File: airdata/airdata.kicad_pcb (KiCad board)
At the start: 2 copper layers, 3 parts, among them U1 SDP32, U3 SDP32, U6 SDP32

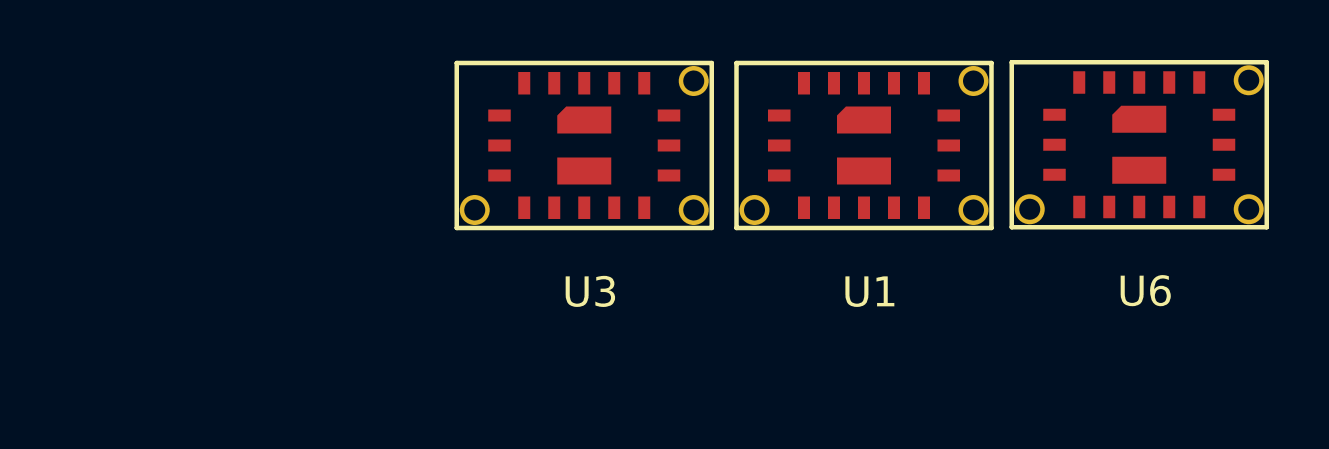
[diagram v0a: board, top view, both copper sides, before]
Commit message: airdata footprints & 3d models
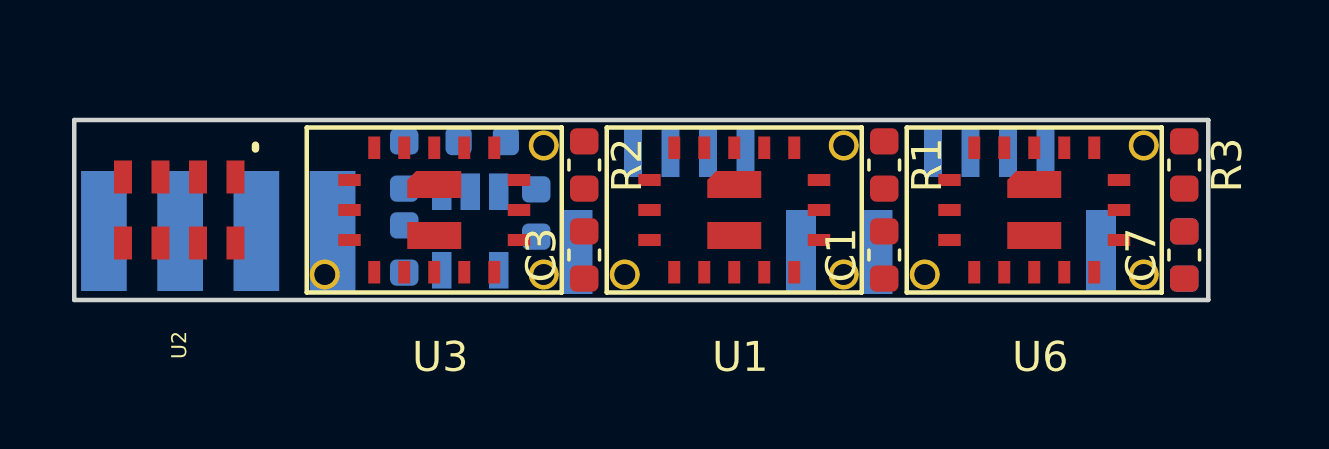
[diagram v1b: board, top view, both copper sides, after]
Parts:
- added C1: 100nF, Capacitor_SMD:C_0603_1608Metric, F.Cu at (55.0, 34.0)
- added C2: 100nF, Capacitor_SMD:C_0603_1608Metric, B.Cu at (65.0, 34.0)
- added C3: 100nF, Capacitor_SMD:C_0603_1608Metric, F.Cu at (45.0, 34.0)
- added C4: 1uF, Capacitor_SMD:C_0603_1608Metric, B.Cu at (41.6, 30.2)
- added C5: 100nF, Capacitor_SMD:C_0603_1608Metric, B.Cu at (39.0, 31.0)
- added C6: 0.01uF, Capacitor_SMD:C_0603_1608Metric, B.Cu at (43.4, 32.6)
- added C7: 100nF, Capacitor_SMD:C_0603_1608Metric, F.Cu at (65.0, 34.0)
- added C8: 10uF, Capacitor_SMD:C_0603_1608Metric, B.Cu at (39.0, 33.8)
- added J1: I2C, Connector_JST:JST_GH_BM04B-GHS-TBT_1x04-1MP_P1.25mm_Vertical, B.Cu at (58.5, 32.5)
- added J2: I2C, Connector_JST:JST_GH_BM04B-GHS-TBT_1x04-1MP_P1.25mm_Vertical, B.Cu at (48.5, 32.5)
- added R1: 0, Resistor_SMD:R_0603_1608Metric, F.Cu at (55.0, 31.0)
- added R2: 1.2k, Resistor_SMD:R_0603_1608Metric, F.Cu at (45.0, 31.0)
- added R3: 2.7k, Resistor_SMD:R_0603_1608Metric, F.Cu at (65.0, 31.0)
- added U2: MS5611-01BA03, footprints:MS5611-01BA, F.Cu at (31.5, 32.5)
- added U4: LT1761-3.3, Package_TO_SOT_SMD:TSOT-23-5, B.Cu at (41.2, 33.2)
- added U5: HSCMRRN001PD2A3, footprints:HSCMRRN001PD2A3-side-mount, B.Cu at (32.8, 33.2)
- moved U3 5.44 mm to (40.0, 32.5)
- moved U1 4.83 mm to (50.0, 32.5)
- moved U6 4.12 mm to (60.0, 32.5)
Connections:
- U1 pad 12: Net-(U1-Pad12) -> (no net)
- U1 pad 13: Net-(U1-Pad13) -> (no net)
- U1 pad 14: Net-(U1-Pad14) -> (no net)
- U1 pad 15: Net-(U1-Pad15) -> (no net)
- U1 pad 16: Net-(U1-Pad16) -> (no net)
- U1 pad 4: Net-(U1-Pad4) -> (no net)
- U3 pad 12: Net-(U3-Pad12) -> (no net)
- U3 pad 13: Net-(U3-Pad13) -> (no net)
- U3 pad 14: Net-(U3-Pad14) -> (no net)
- U3 pad 15: Net-(U3-Pad15) -> (no net)
- U3 pad 16: Net-(U3-Pad16) -> (no net)
- U3 pad 4: Net-(U3-Pad4) -> (no net)
- U6 pad 12: Net-(U6-Pad12) -> (no net)
- U6 pad 13: Net-(U6-Pad13) -> (no net)
- U6 pad 14: Net-(U6-Pad14) -> (no net)
- U6 pad 15: Net-(U6-Pad15) -> (no net)
- U6 pad 16: Net-(U6-Pad16) -> (no net)
- U6 pad 4: Net-(U6-Pad4) -> (no net)
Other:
- board outline added: 37.8 x 6 mm

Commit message: airdata & power supply pcb
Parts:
- moved C4 3.12 mm to (43.6, 32.6), turned to 270 degrees
- moved C6 2.90 mm to (41.4, 34.7), turned to 0 degrees
- moved U4 1.41 mm to (41.4, 31.8)
- moved J1 0.60 mm to (59.1, 32.5)
- moved J2 0.50 mm to (49.0, 32.5)
- moved U2 0.10 mm to (31.6, 32.5)
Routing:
- net GND: track 0.00 -> 111.3 mm, vias 0 -> 8
- net +3V3: track 0.00 -> 70.6 mm, vias 0 -> 7
- net /SDA: track 0.00 -> 47.0 mm, vias 0 -> 4
- net /SCL: track 0.00 -> 37.0 mm, vias 0 -> 4
- net +5V: track 0.00 -> 33.9 mm, vias 0 -> 2
- net Net-(R3-Pad1): track 0.00 -> 6.54 mm, vias 0 -> 2
- net Net-(R1-Pad1): track 0.00 -> 4.20 mm
- net Net-(R2-Pad1): track 0.00 -> 4.12 mm
- net Net-(C6-Pad2): track 0.00 -> 1.70 mm
- added copper zone on In1.Cu, net GND
- added copper zone on In2.Cu, net GND
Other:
- board size 37.8 x 6 mm -> 38.2 x 6 mm
- copper layers 2 -> 4
- rule trace_min: 0.2 -> 0.152
- rule via_min_size: 0.4 -> 0.6
